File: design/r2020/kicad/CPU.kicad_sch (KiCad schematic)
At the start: 15 parts, among them IC1 MC68020RC, IC8 ATF16V8BQL, Q2 5H8ET-20.000

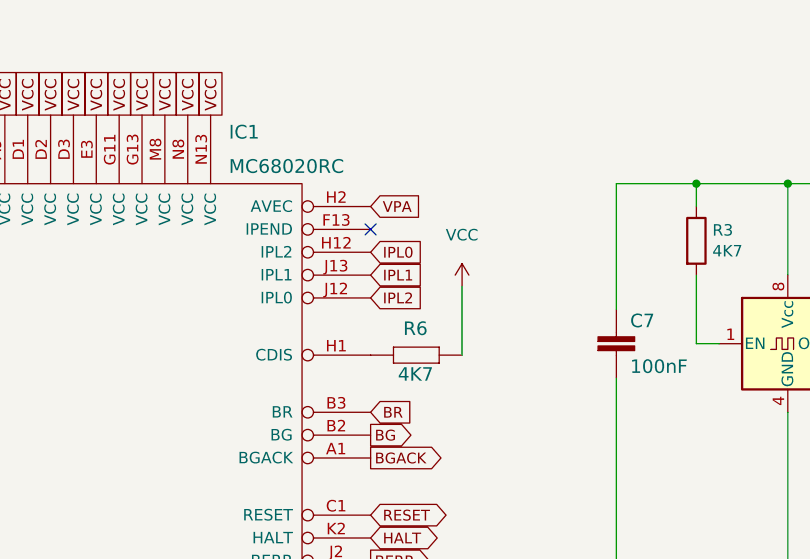
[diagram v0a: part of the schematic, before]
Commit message: Fix IPLn mixup
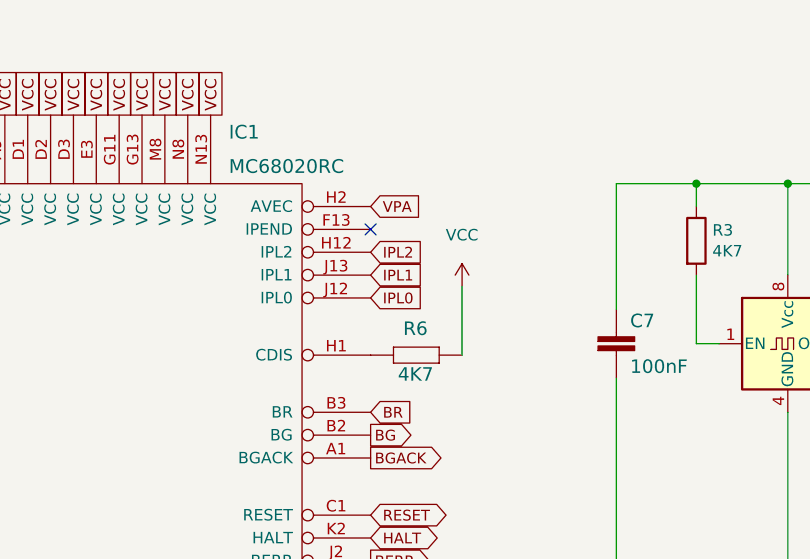
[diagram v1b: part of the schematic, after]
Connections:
- net IPL0: now also IC1.J12 (IPL0); no longer IC1.H12 (IPL2)
- net IPL2: now also IC1.H12 (IPL2); no longer IC1.J12 (IPL0)
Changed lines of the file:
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@@
     )
   )
-  (global_label "IPL0" (shape input) (at 120.65 48.26 0) (fields_autoplaced)
-    (effects (font (size 1.1938 1.1938)) (justify left))
-    (property "Intersheet References" "${INTERSHEET_REFS}" (id 0) (at 215.9 133.35 0)
+  (global_label "IPL0" (shape input) (at 120.65 53.34 0) (fields_autoplaced)
+    (effects (font (size 1.1938 1.1938)) (justify left))
+    (property "Intersheet References" "${INTERSHEET_REFS}" (id 0) (at 215.9 138.43 0)
       (effects (font (size 1.27 1.27)) hide)
     )
@@
     )
   )
-  (global_label "IPL2" (shape input) (at 120.65 53.34 0) (fields_autoplaced)
-    (effects (font (size 1.1938 1.1938)) (justify left))
-    (property "Intersheet References" "${INTERSHEET_REFS}" (id 0) (at 215.9 143.51 0)
-      (effects (font (size 1.27 1.27)) hide)
-    )
+  (global_label "IPL2" (shape input) (at 120.65 48.26 0) (fields_autoplaced)
+    (effects (font (size 1.1938 1.1938)) (justify left))
+    (property "Intersheet References" "${INTERSHEET_REFS}" (id 0) (at 215.9 138.43 0)
+      (effects (font (size 1.27 1.27)) hide)
+    )

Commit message: More cleanup
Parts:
- removed R5, R6, R7, R9: 4K7, rosco_m68k:0207_10, symbol rosco_m68k-eagle-import:R-EU_0207_10
- added RN1: 4K7, Resistor_THT:R_Array_SIP9, symbol Device:R_Network08
- renumbered RN1 to RN2, RN2 to RN3
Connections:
- net BGACK: now also RN1.3 (R2)
- net BR: now also RN1.2 (R1)
- net VCC: now also RN1.1 (common)
- net DBEN: now reaches IC1.G3 (DBEN)
- net DBEN: now also RN1.9 (R8); no longer R4.1
- net DSACK0: now reaches IC1.H3 (DSACK0)
- net DSACK0: now also R4.1
- net CDIS: now reaches IC1.H1 (CDIS)
- net CDIS: now also RN1.8 (R7)
- new net IRQ2: RN1.6 (R5)
- new net IRQ3: RN1.4 (R3)
- new net IRQ5: RN1.5 (R4)
- new net IRQ6: RN1.7 (R6)
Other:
- moved on the sheet: R10, RN2, RN3
